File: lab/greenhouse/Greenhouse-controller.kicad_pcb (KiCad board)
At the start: 2 copper layers, 100 x 90 mm, 10 parts, among them U1 atmega328p

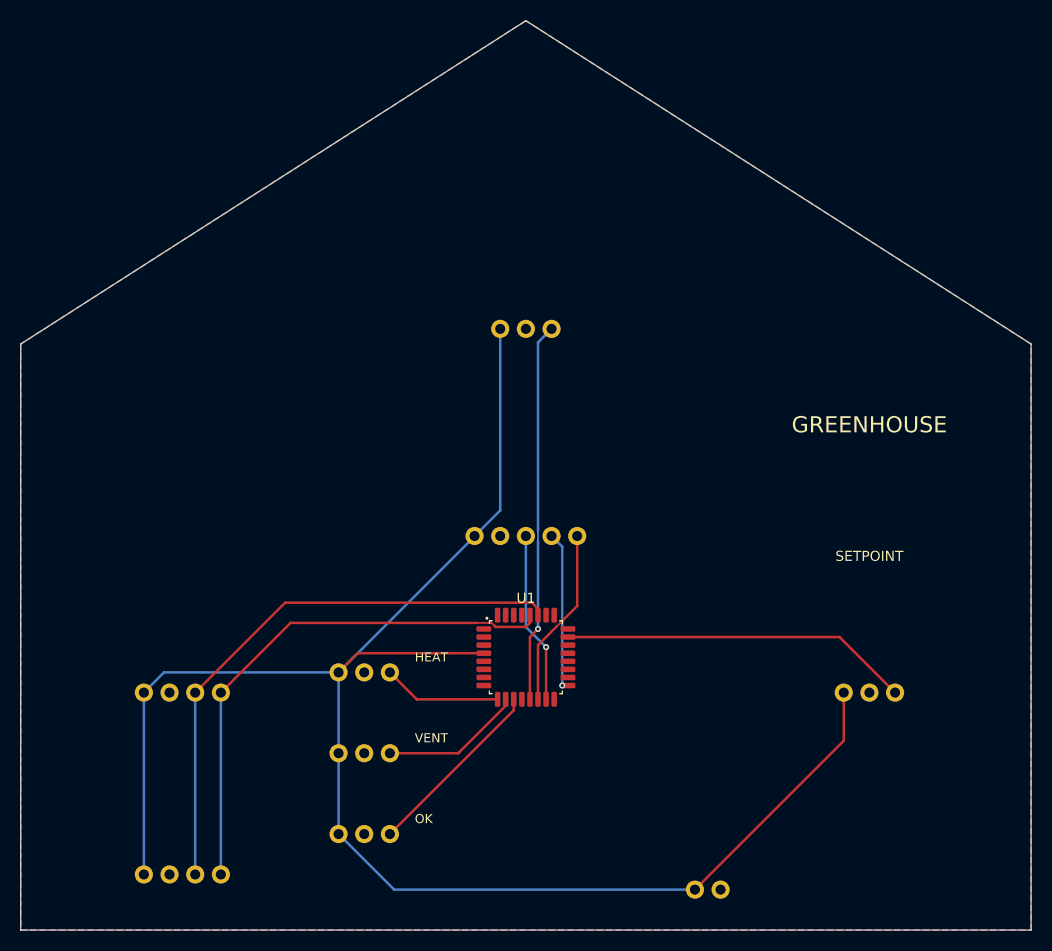
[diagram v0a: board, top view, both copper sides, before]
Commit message: lab: every board is a real board: an Arduino Nano and registry parts, routed, ready to order
The lab boards ran on simulation-only envelopes (labMcu, labDisplay, a battery). Now each is
an Arduino Nano on two sockets on the back (flashed over its USB, the image the app builds),
its lights LEDs through 1 kΩ, its knobs PTV09A pots, its display the MAX7219 eight-digit
module, its sensors an SHT31 and an SCD40 with their datasheets' support circuits, the FTDI
header for the serial console; the servo boards take 5 V on a screw terminal with a bulk
capacitor. All ten check complete with no errors or warnings, their firmware unchanged
(serial-device now on the 328P), and run in the lab without a fault (3 s each, dev host).

The registry: every interactive board must be ready to order and flash (publish.mjs refuses
one that is not; status simulation-only removed).

Claude-Session: https://claude.ai/code/session_01ATmMmxyrWxFwR3nTdXUrcx
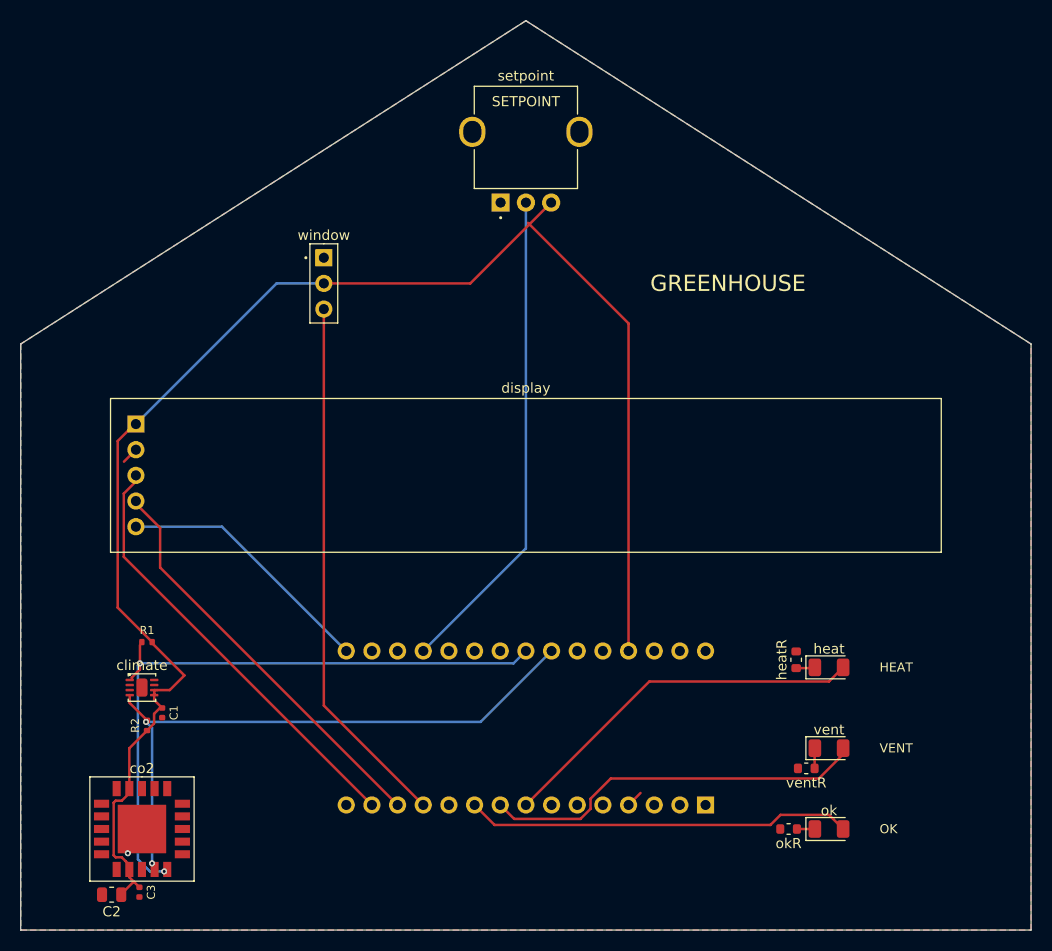
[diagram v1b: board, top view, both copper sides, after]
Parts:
- removed battery: battery, Regulated battery module
- removed the climate at (116.0, 173.0)
- removed the display at (150.0, 155.0)
- removed the heat at (134.0, 173.0)
- removed the ok at (134.0, 189.0)
- removed the setpoint at (184.0, 172.0)
- removed the vent at (134.0, 181.0)
- removed the window at (150.0, 136.0)
- added C1: 100nF, C_0402_1005Metric, F.Cu at (114.0, 178.5)
- added C2: 10uF, C_0805_2012Metric, F.Cu at (109.0, 196.5)
- added C3: 100nF, C_0402_1005Metric, F.Cu at (111.8, 196.2)
- added R1: 10kohm, R_0402_1005Metric, F.Cu at (112.5, 171.5)
- added R2: 10kohm, R_0402_1005Metric, F.Cu at (112.5, 179.8)
- added climate: SHT31-DIS-B2.5kS, DFN-8-1EP_2.5x2.5mm_P0.5mm_EP1.1x1.8mm, F.Cu at (112.0, 176.0)
- added display: MAX7219 8-digit 7-segment LED display module, MAX7219_8digit_Module_Socket_1x05_P2.54mm, F.Cu at (150.0, 155.0)
- added heat: red, LED_1206_3216Metric, F.Cu at (180.0, 174.0)
- added heatR: 1kohm, R_0603_1608Metric, F.Cu at (176.8, 173.2)
- added ok: green, LED_1206_3216Metric, F.Cu at (180.0, 190.0)
- added okR: 1kohm, R_0603_1608Metric, F.Cu at (176.0, 190.0)
- added setpoint: PTV09A-4020F-B103, Potentiometer_Bourns_PTV09A-4_Vertical, F.Cu at (150.0, 128.0)
- added vent: orange, LED_1206_3216Metric, F.Cu at (180.0, 182.0)
- added ventR: 1kohm, R_0603_1608Metric, F.Cu at (177.8, 184.0)
- added window: RC servo header, 1 x 3 pins, 2.54 mm, PinHeader_1x03_P2.54mm_Vertical, F.Cu at (130.0, 136.0)
- U1: value atmega328p -> A000005; footprint TQFP-32_7x7mm_P0.8mm -> Arduino_Nano_Socket_2x15_P2.54mm_W15.24mm; moved to B.Cu
- co2: value scd40 -> SCD40-D-R2; footprint SCD40 module -> LGA-21_10.1x10.1mm_SCD4x_20_pads_and_a_centre_pad
- moved U1 7.00 mm to (150.0, 180.0), turned to 90 degrees
- moved co2 4.12 mm to (112.0, 190.0)
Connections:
- U1 pad 10: VENT -> OK
- U1 pad 11: OK -> (no net)
- U1 pad 12: (no net) -> WINDOW
- U1 pad 13: WINDOW -> LOAD
- U1 pad 14: LOAD -> MOSI
- U1 pad 15: MOSI -> (no net)
- U1 pad 16: (no net) -> SCK
- U1 pad 17: SCK -> (no net)
- U1 pad 19: (no net) -> SETPOINT
- U1 pad 23: SETPOINT -> SDA
- U1 pad 24: (no net) -> SCL
- U1 pad 27: SDA -> V5
- U1 pad 28: SCL -> (no net)
- U1 pad 29: (no net) -> GND
- U1 pad 3: GND -> (no net)
- U1 pad 4: V5 -> GND
- U1 pad 8: (no net) -> HEAT
- U1 pad 9: HEAT -> VENT
- co2 pad 1: V5 -> (no net)
- co2 pad 2: GND -> (no net)
- co2 pad 3: SDA -> (no net)
- co2 pad 4: SCL -> (no net)
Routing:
- net MOSI: track 17.0 -> 43.3 mm, vias 1 -> 0
- net HEAT: track 11.8 -> 37.0 mm
- net VENT: track 14.0 -> 38.3 mm
- net LOAD: track 17.8 -> 40.8 mm
- net OK: track 18.4 -> 38.3 mm
- net V5: track 173.0 -> 154.3 mm
- net WINDOW: track 37.5 -> 53.2 mm, vias 1 -> 0
- net SETPOINT: track 34.7 -> 48.6 mm
- net SCK: track 15.2 -> 25.9 mm, vias 1 -> 0
- net SDA: track 56.5 -> 65.0 mm, vias 0 -> 2
- net SCL: track 54.1 -> 60.5 mm, vias 0 -> 2
- net GND: track 0.00 -> 3.35 mm, vias 0 -> 1
- net VENT_K: track 0.00 -> 2.01 mm
- net HEAT_K: track 0.00 -> 1.88 mm
- net OK_K: track 0.00 -> 1.78 mm
